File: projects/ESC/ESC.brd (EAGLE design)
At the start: 139.7 x 38.1 mm, 93 parts, among them J1 1755529, J2 1755529, J3 1755529, J4 1755529, U1 STM32F405RGT6, U10 CSD88584Q5DCT, U11 CSD88584Q5DCT, U12 CSD88584Q5DCT, U13 CSD88584Q5DCT, U14 SN74CBTLV3257PWR, U15 CSD88584Q5DCT, U16 CSD88584Q5DCT, U17 CSD88584Q5DCT, U2 CSD88584Q5DCT, U3 CSD88584Q5DCT, U4 CSD88584Q5DCT, U8 CSD88584Q5DCT, U9 CSD88584Q5DCT, Y1 ECS-80-S-4X

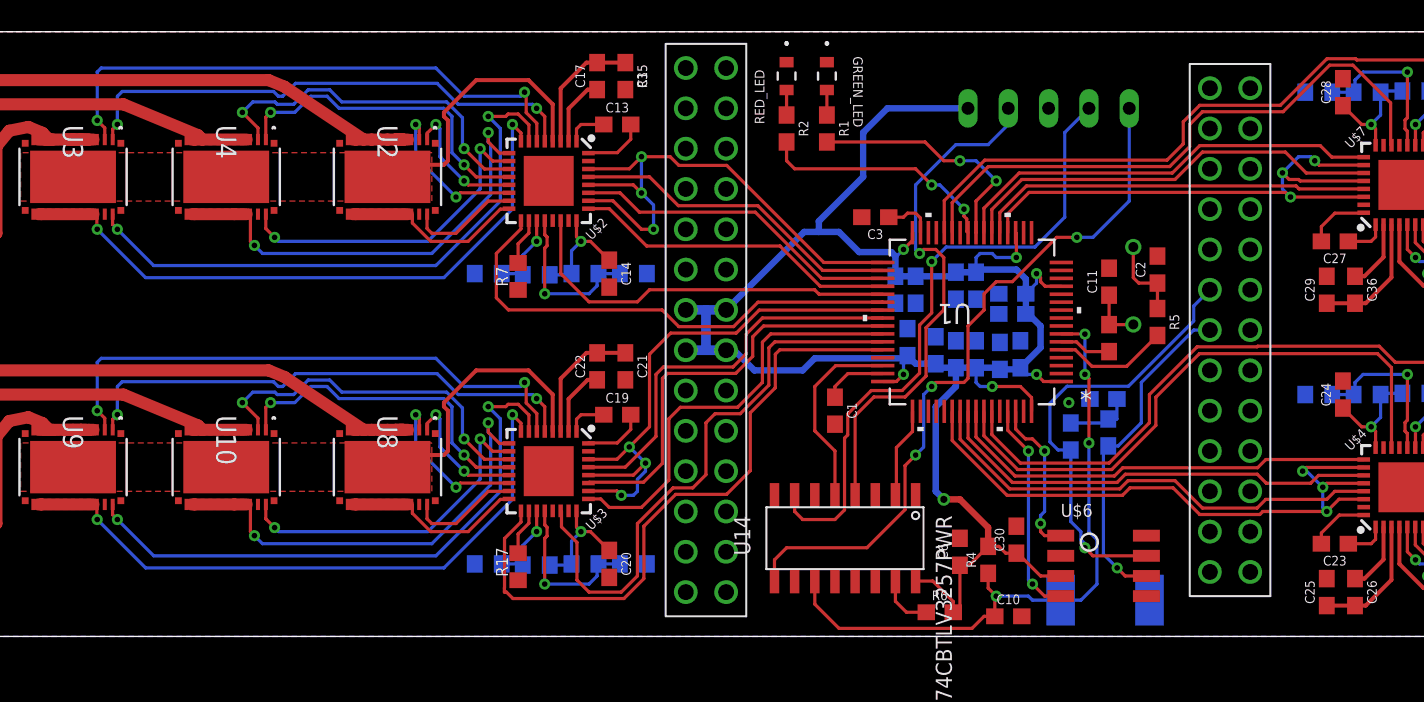
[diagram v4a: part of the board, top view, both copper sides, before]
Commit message: Made naming changes to VM and SL to 12 and GND
Changed the names for the motor voltage sources to 12 and gnd. only thing left is to connect the 12 volt supply to the 6-packs, might need another layer.
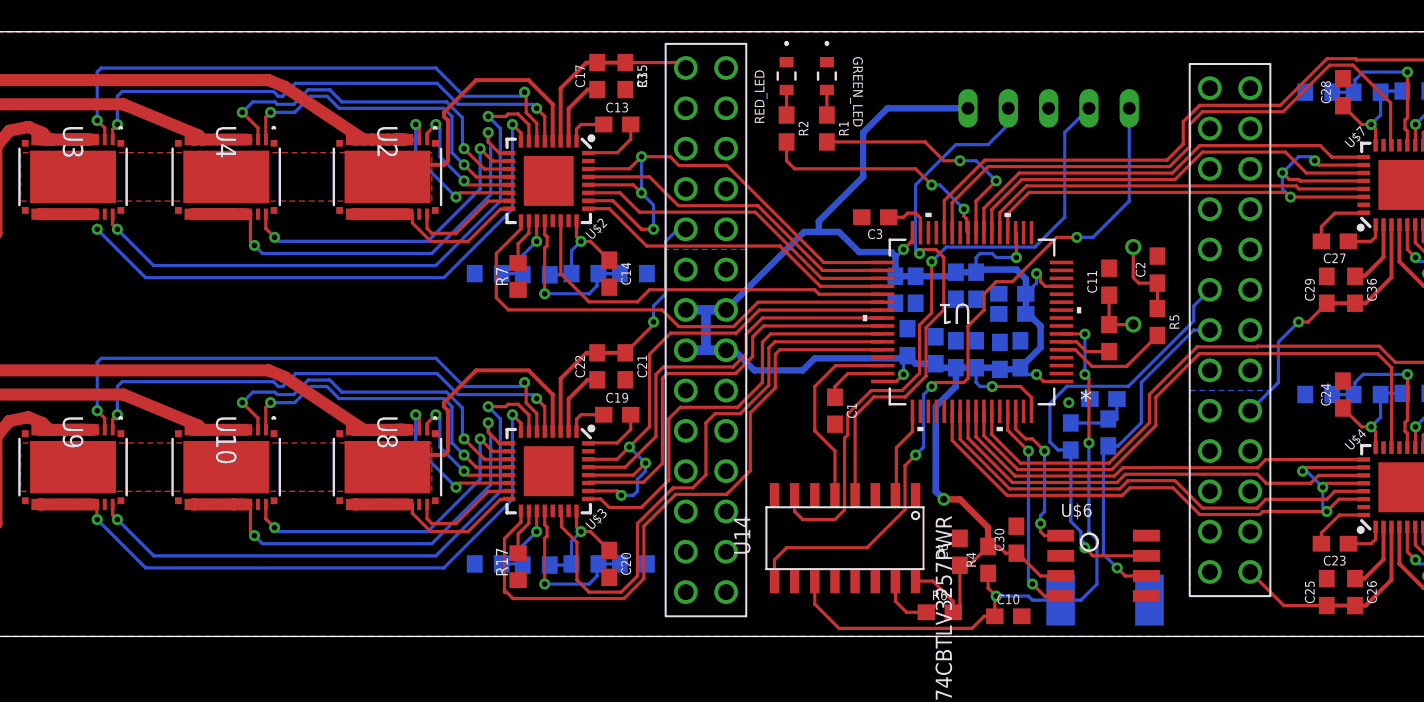
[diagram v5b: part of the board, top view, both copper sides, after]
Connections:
- removed net SLA_1: U$2.8, U3.12, U3.13, U3.14, U3.15, U3.16, U3.17, U3.18, U3.19, U3.20
- removed net SLA_2: U$3.8, U9.12, U9.13, U9.14, U9.15, U9.16, U9.17, U9.18, U9.19, U9.20
- removed net SLA_3: U$4.8, U12.12, U12.13, U12.14, U12.15, U12.16, U12.17, U12.18, U12.19, U12.20
- removed net SLA_4: U$7.8, U16.12, U16.13, U16.14, U16.15, U16.16, U16.17, U16.18, U16.19, U16.20
- removed net SLB_1: U$2.9, U4.12, U4.13, U4.14, U4.15, U4.16, U4.17, U4.18, U4.19, U4.20
- removed net SLB_2: U$3.9, U10.12, U10.13, U10.14, U10.15, U10.16, U10.17, U10.18, U10.19, U10.20
- removed net SLB_3: U$4.9, U13.12, U13.13, U13.14, U13.15, U13.16, U13.17, U13.18, U13.19, U13.20
- removed net SLB_4: U$7.9, U17.12, U17.13, U17.14, U17.15, U17.16, U17.17, U17.18, U17.19, U17.20
- removed net SLC_1: U$2.16, U2.12, U2.13, U2.14, U2.15, U2.16, U2.17, U2.18, U2.19, U2.20
- removed net SLC_2: U$3.16, U8.12, U8.13, U8.14, U8.15, U8.16, U8.17, U8.18, U8.19, U8.20
- removed net SLC_3: U$4.16, U11.12, U11.13, U11.14, U11.15, U11.16, U11.17, U11.18, U11.19, U11.20
- removed net SLC_4: U$7.16, U15.12, U15.13, U15.14, U15.15, U15.16, U15.17, U15.18, U15.19, U15.20
- removed net VM_1: C15.1, C17.2, U$2.3, U$2.4, U2.27, U3.27, U4.27
- removed net VM_2: C21.1, C22.2, U$3.3, U$3.4, U10.27, U8.27, U9.27
- removed net VM_3: C25.1, C26.2, U$4.3, U$4.4, U11.27, U12.27, U13.27
- removed net VM_4: C29.1, C36.2, U$7.3, U$7.4, U15.27, U16.27, U17.27
- net +12V: now also C15.1, C17.2, C21.1, C22.2, C25.1, C26.2, C29.1, C36.2, U$2.3, U$2.4, U$3.3, U$3.4, U$4.3, U$4.4, U$7.3, U$7.4, U10.27, U11.27, U12.27, U13.27, U15.27, U16.27, U17.27, U2.27, U3.27, U4.27, U8.27, U9.27
- net GND: now also U$2.16, U$2.8, U$2.9, U$3.16, U$3.8, U$3.9, U$4.16, U$4.8, U$4.9, U$7.16, U$7.8, U$7.9, U10.12, U10.13, U10.14, U10.15, U10.16, U10.17, U10.18, U10.19, U10.20, U11.12, U11.13, U11.14, U11.15, U11.16, U11.17, U11.18, U11.19, U11.20, U12.12, U12.13, U12.14, U12.15, U12.16, U12.17, U12.18, U12.19, U12.20, U13.12, U13.13, U13.14, U13.15, U13.16, U13.17, U13.18, U13.19, U13.20, U15.12, U15.13, U15.14, U15.15, U15.16, U15.17, U15.18, U15.19, U15.20, U16.12, U16.13, U16.14, U16.15, U16.16, U16.17, U16.18, U16.19, U16.20, U17.12, U17.13, U17.14, U17.15, U17.16, U17.17, U17.18, U17.19, U17.20, U2.12, U2.13, U2.14, U2.15, U2.16, U2.17, U2.18, U2.19, U2.20, U3.12, U3.13, U3.14, U3.15, U3.16, U3.17, U3.18, U3.19, U3.20, U4.12, U4.13, U4.14, U4.15, U4.16, U4.17, U4.18, U4.19, U4.20, U8.12, U8.13, U8.14, U8.15, U8.16, U8.17, U8.18, U8.19, U8.20, U9.12, U9.13, U9.14, U9.15, U9.16, U9.17, U9.18, U9.19, U9.20
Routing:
- net GND: track 0.00 -> 323.3 mm, vias 0 -> 16
- net +12V: track 0.00 -> 132.9 mm, vias 0 -> 2
- net SLA_4: track 40.3 -> 0.00 mm, vias 2 -> 0
- net SLA_3: track 40.3 -> 0.00 mm, vias 2 -> 0
- net SLA_1: track 40.3 -> 0.00 mm, vias 2 -> 0
- net SLA_2: track 40.3 -> 0.00 mm, vias 2 -> 0
- net SLB_1: track 29.3 -> 0.00 mm, vias 2 -> 0
- net SLB_2: track 29.3 -> 0.00 mm, vias 2 -> 0
- net SLB_4: track 29.3 -> 0.00 mm, vias 2 -> 0
- net SLB_3: track 29.3 -> 0.00 mm, vias 2 -> 0
- net VM_2: track 26.1 -> 0.00 mm
- net VM_1: track 26.1 -> 0.00 mm
- net VM_4: track 26.1 -> 0.00 mm
- net VM_3: track 26.1 -> 0.00 mm
- net SLC_1: track 11.5 -> 0.00 mm
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- added copper zone on layer 1, net +12V
- added copper zone on layer 16, net +12V
- removed copper zone on layer 1, net VM_1
- removed copper zone on layer 1, net VM_2
- removed copper zone on layer 1, net VM_3
- removed copper zone on layer 1, net VM_4

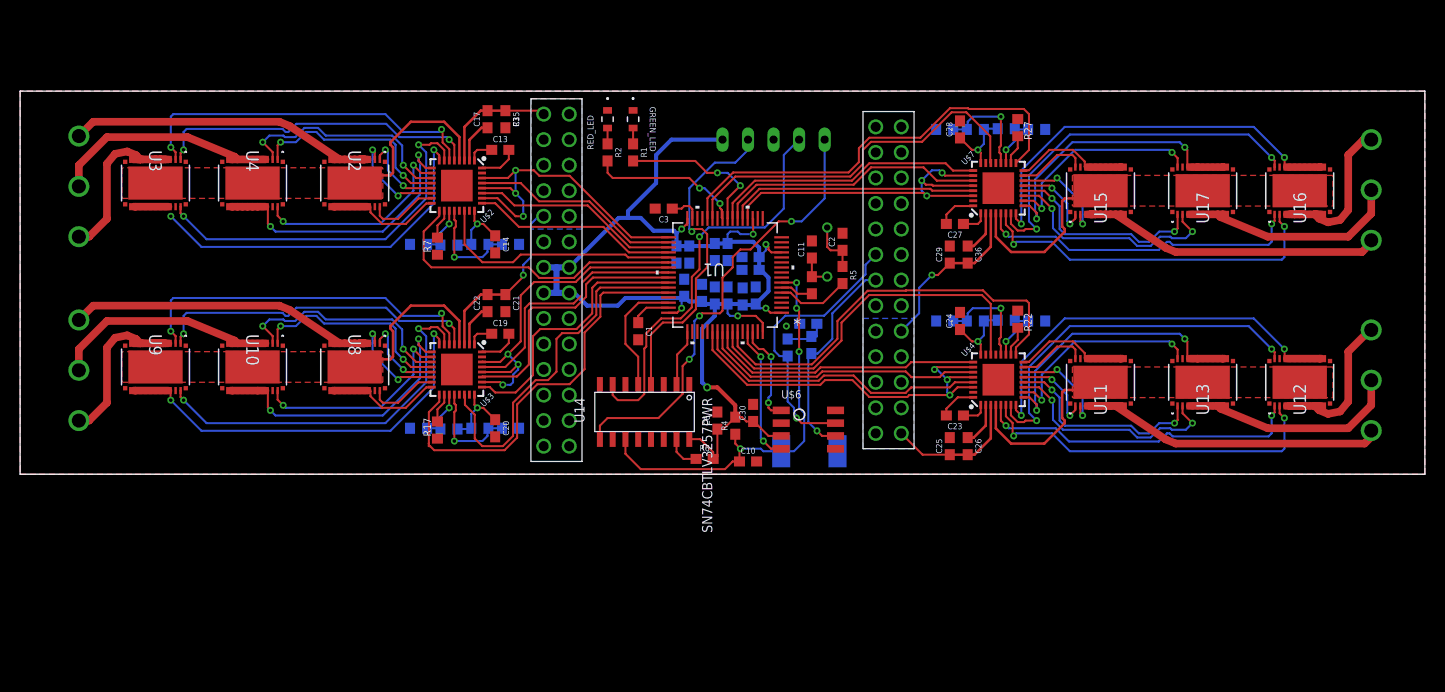
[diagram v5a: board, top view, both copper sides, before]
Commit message: Connected +12V to the motor drivers.
Used 30 mil traces. If 3 or 4 layer board design is decided on in the future, revert to the version before this one.
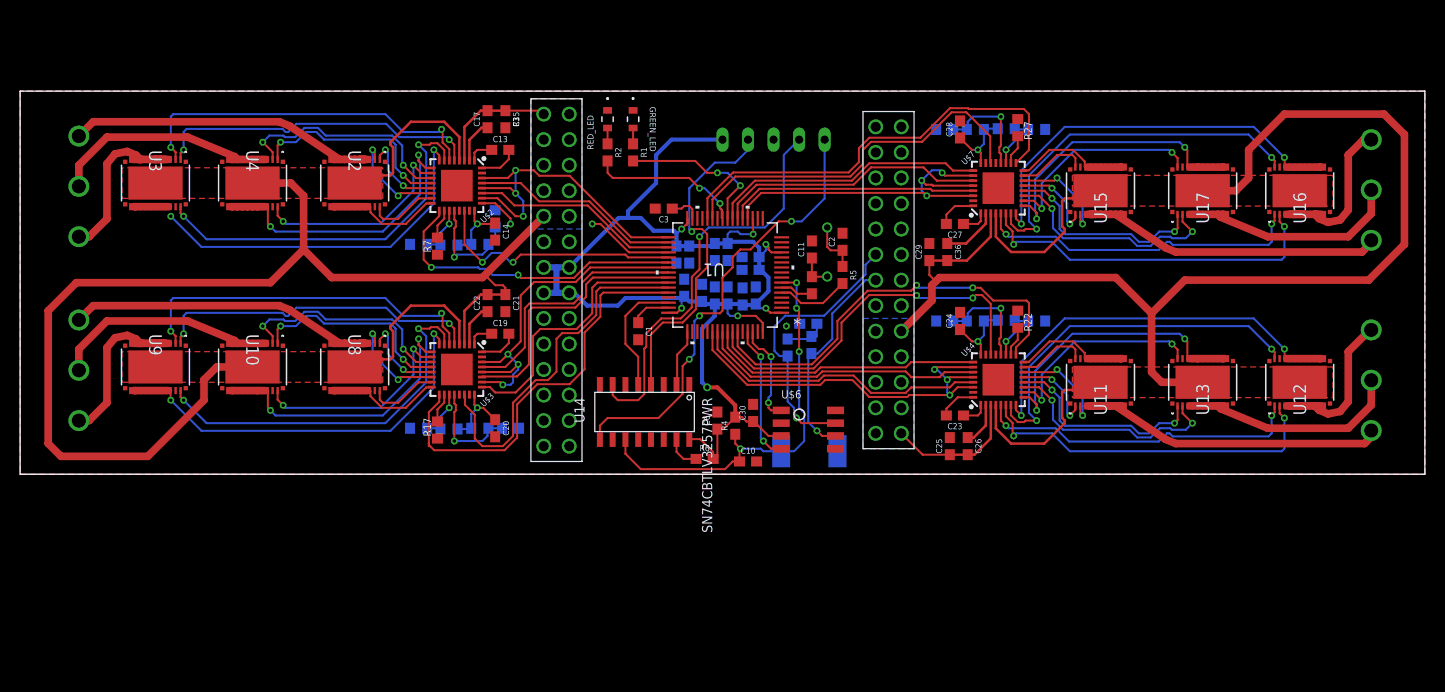
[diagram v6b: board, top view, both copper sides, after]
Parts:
- moved R11 2.96 mm to (47.2, 25.4), turned to 270 degrees
- moved C29 2.05 mm to (90.4, 22.1)
- moved C36 2.05 mm to (92.2, 22.1)
- moved C14 1.27 mm to (47.2, 24.1)
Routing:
- net +12V: track 132.9 -> 331.9 mm, vias 2 -> 0
- net INHA_1: track 20.6 -> 12.8 mm, vias 0 -> 2
- net N$33: track 4.35 -> 5.68 mm
- net EN_1: track 24.8 -> 25.6 mm, vias 0 -> 2
- net FAULT_3: track 41.5 -> 41.9 mm, vias 0 -> 2
- net EN_3: track 37.6 -> 37.8 mm, vias 0 -> 2
- net FAULT_1: vias 0 -> 2

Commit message: Revert "Connected +12V to the motor drivers."
This reverts commit 0ece1cb6e85931862ee2ef5365700be815a9b472.
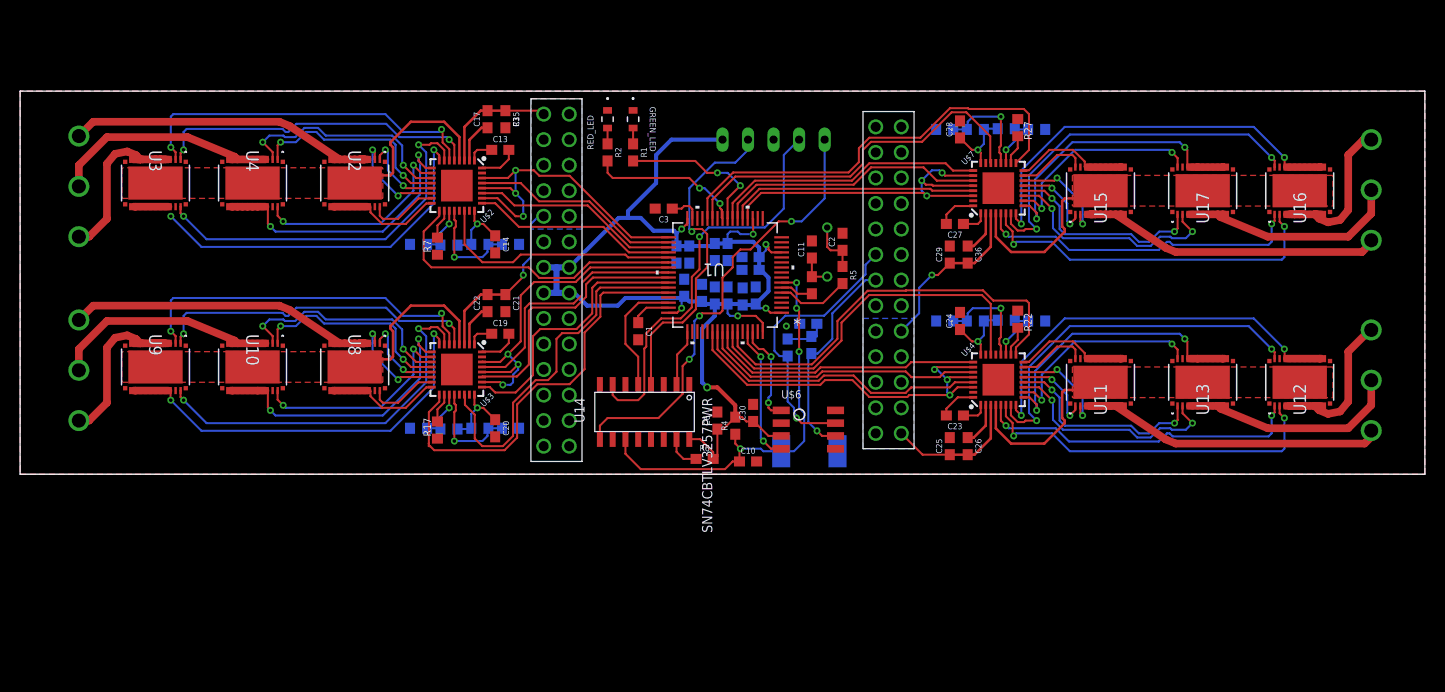
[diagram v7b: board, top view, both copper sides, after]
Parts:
- moved R11 2.96 mm to (48.8, 22.9), turned to 0 degrees
- moved C29 2.05 mm to (92.5, 21.8)
- moved C36 2.05 mm to (94.2, 21.8)
- moved C14 1.27 mm to (47.2, 22.9)
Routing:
- net +12V: track 331.9 -> 132.9 mm, vias 0 -> 2
- net INHA_1: track 12.8 -> 20.6 mm, vias 2 -> 0
- net N$33: track 5.68 -> 4.35 mm
- net EN_1: track 25.6 -> 24.8 mm, vias 2 -> 0
- net FAULT_3: track 41.9 -> 41.5 mm, vias 2 -> 0
- net EN_3: track 37.8 -> 37.6 mm, vias 2 -> 0
- net FAULT_1: vias 2 -> 0

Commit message: Added 2 layers and made some polygons for +12V
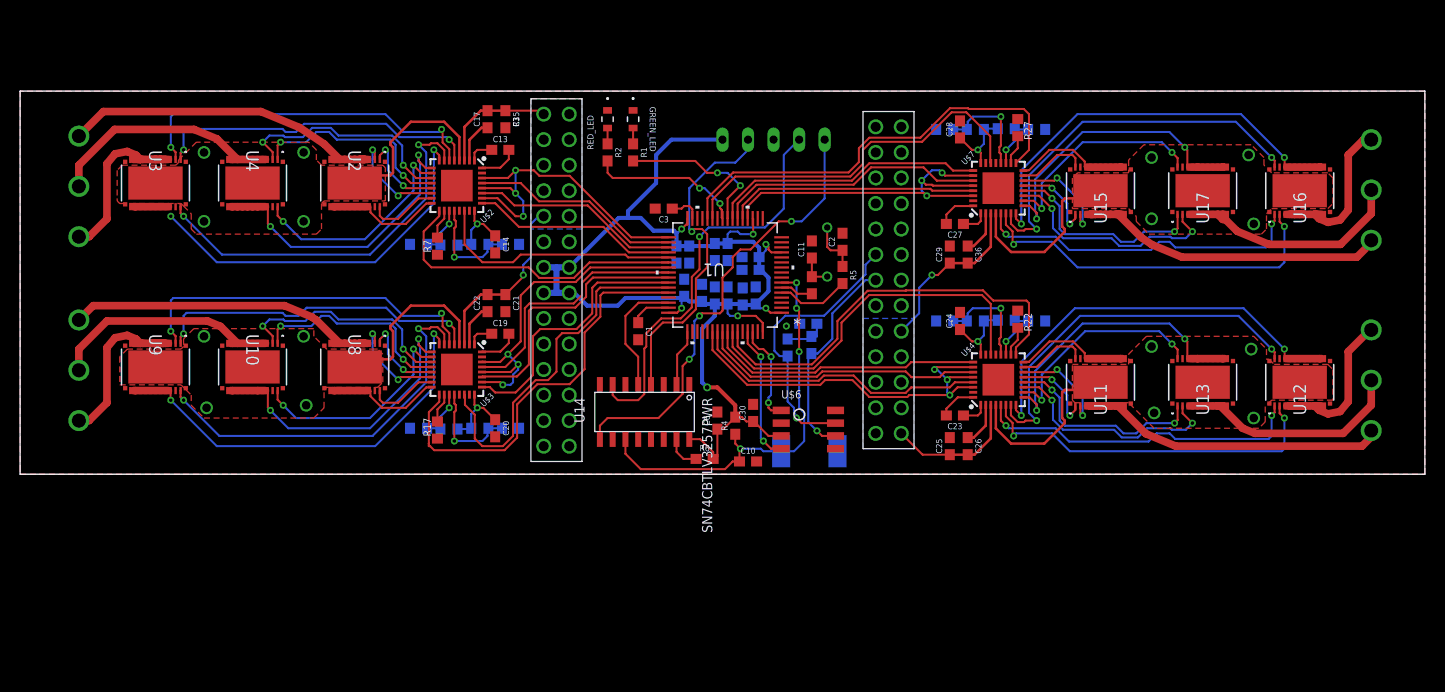
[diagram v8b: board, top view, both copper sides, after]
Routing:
- net GND: track 323.3 -> 331.7 mm
- net GLB_1: track 20.8 -> 22.1 mm
- net GLA_1: track 37.4 -> 38.7 mm
- net GLA_4: track 37.4 -> 38.5 mm
- net GLA_2: track 37.4 -> 38.5 mm
- net SHA_4: track 35.7 -> 36.7 mm
- net PHASE_B1: track 23.0 -> 23.9 mm
- net GLB_3: track 20.8 -> 21.6 mm
- net GLB_2: track 20.8 -> 21.6 mm
- net GLA_3: track 37.4 -> 38.3 mm
- net PHASE_C1: track 31.8 -> 32.6 mm
- net PHASE_B4: track 22.6 -> 23.3 mm
- net PHASE_B3: track 22.7 -> 23.4 mm
- net GLB_4: track 20.8 -> 21.4 mm
- net PHASE_C4: track 31.4 -> 31.9 mm
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- added copper zone on layer 2, net +12V
